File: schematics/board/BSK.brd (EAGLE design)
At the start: 94 x 94 mm, 47 parts

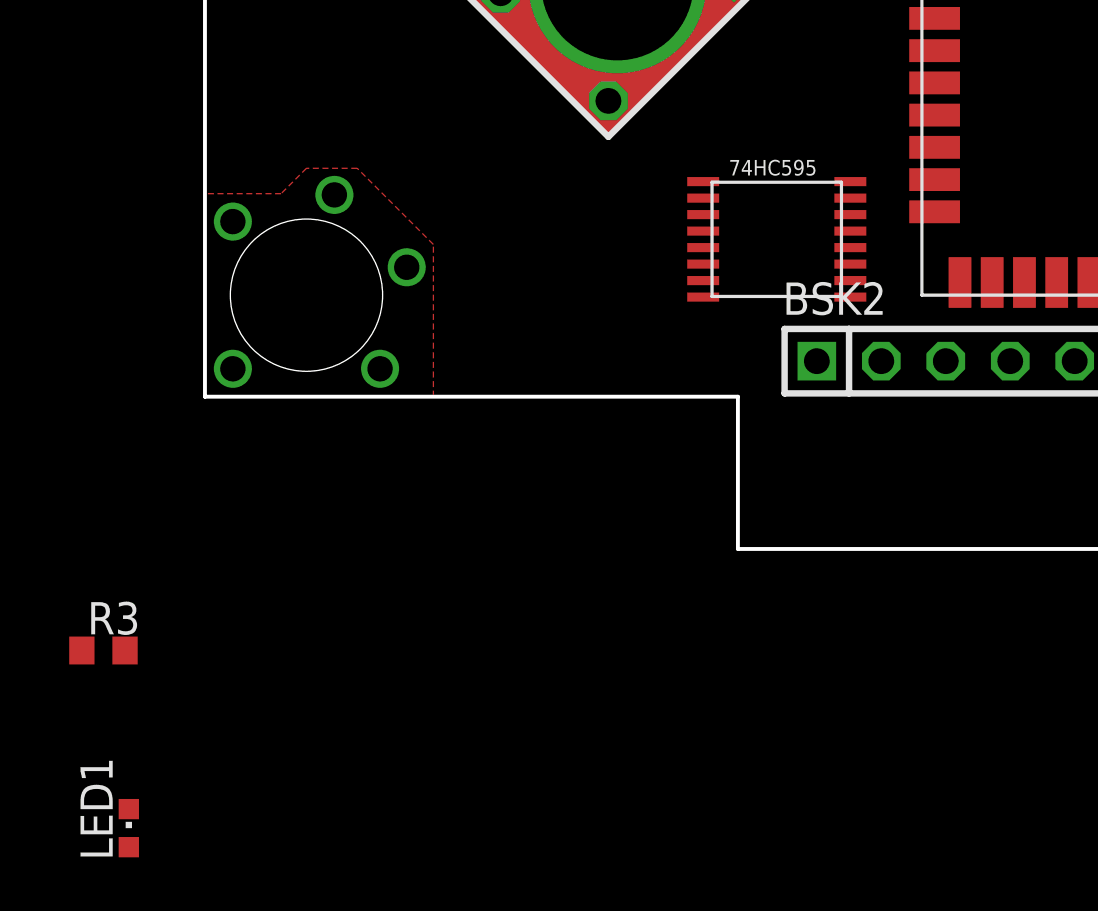
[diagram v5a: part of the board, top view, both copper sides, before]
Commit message: обновлена схема БКУ
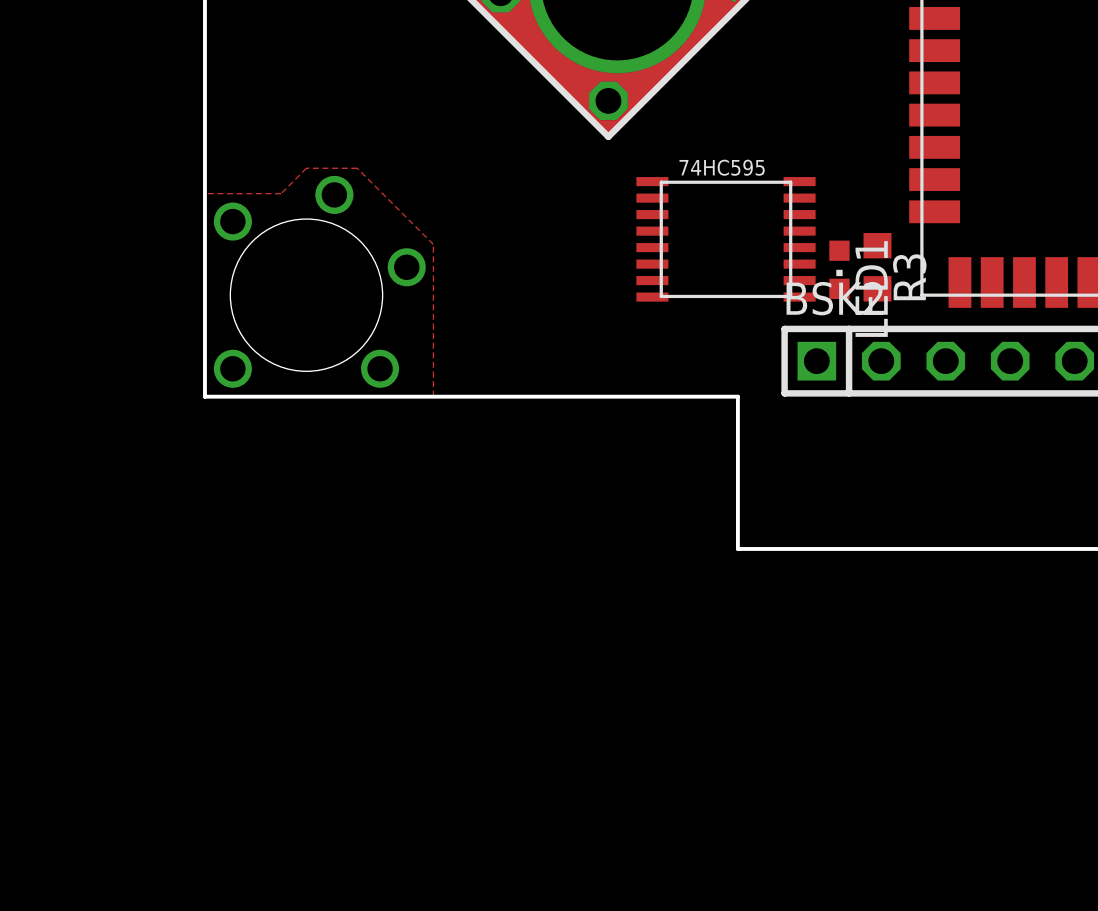
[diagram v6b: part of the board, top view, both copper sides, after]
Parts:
- moved LED1 35.6 mm to (31.0, 11.0), turned to 180 degrees
- moved R3 34.0 mm to (32.5, 11.1), turned to 270 degrees
- moved U$15 2.00 mm to (26.5, 12.2)
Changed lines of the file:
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@@
 <attribute name="VALUE" x="82.635" y="56.105" size="1.27" layer="27" rot="R180"/>
 </element>
-<element name="U$15" library="CanCubeSat" package="74HC595" value="74HC595" x="28.53" y="12.2" smashed="yes"/>
+<element name="U$15" library="CanCubeSat" package="74HC595" value="74HC595" x="26.53" y="12.2" smashed="yes"/>
 <element name="U$17" library="CanCubeSat" package="74HC595" value="74HC595" x="79.53" y="33.85" smashed="yes"/>
 <element name="BSK3" library="pinheadCS" package="1X12" value="" x="86.6" y="47" smashed="yes" rot="R90">
@@
 </element>
 <element name="U$22" library="CanCubeSat" package="FS8205A+" value="FS8205A+" x="78.8" y="55.3" smashed="yes"/>
-<element name="R3" library="resistor" library_urn="urn:adsk.eagle:library:348" package="R0603" package3d_urn="urn:adsk.eagle:package:23555/3" value="2k" x="2" y="-4" smashed="yes">
-<attribute name="NAME" x="1.365" y="-3.365" size="1.27" layer="25"/>
-<attribute name="VALUE" x="1.365" y="-5.905" size="1.27" layer="27"/>
-</element>
-<element name="LED1" library="led" library_urn="urn:adsk.eagle:library:259" package="CHIPLED_0603" package3d_urn="urn:adsk.eagle:package:15822/2" value="" x="3" y="-11" smashed="yes">
-<attribute name="NAME" x="2.365" y="-12.27" size="1.27" layer="25" rot="R90"/>
-<attribute name="POPULARITY" value="28" x="-3" y="-4" size="1.778" layer="27" display="off"/>
-<attribute name="VALUE" x="4.905" y="-12.27" size="1.27" layer="27" rot="R90"/>
+<element name="R3" library="resistor" library_urn="urn:adsk.eagle:library:348" package="R0603" package3d_urn="urn:adsk.eagle:package:23555/3" value="2k" x="32.5" y="11.1" smashed="yes" rot="R270">
+<attribute name="NAME" x="33.135" y="11.735" size="1.27" layer="25" rot="R270"/>
+<attribute name="VALUE" x="30.595" y="11.735" size="1.27" layer="27" rot="R270"/>
+</element>
+<element name="LED1" library="led" library_urn="urn:adsk.eagle:library:259" package="CHIPLED_0603" package3d_urn="urn:adsk.eagle:package:15822/2" value="" x="31" y="11" smashed="yes" rot="R180">
+<attribute name="NAME" x="31.635" y="12.27" size="1.27" layer="25" rot="R270"/>
+<attribute name="POPULARITY" value="28" x="37" y="4" size="1.778" layer="27" rot="R180" display="off"/>
+<attribute name="VALUE" x="29.095" y="12.27" size="1.27" layer="27" rot="R270"/>
 </element>
 </elements>
@@
 <wire x1="82.43" y1="32.225" x2="71.43" y2="13.805" width="0" layer="19" extent="1-1"/>
 <wire x1="82.43" y1="36.125" x2="82.43" y2="32.225" width="0" layer="19" extent="1-1"/>
-<wire x1="31.43" y1="14.475" x2="50.99" y2="27.5" width="0" layer="19" extent="1-1"/>
-<wire x1="31.43" y1="10.575" x2="31.43" y2="14.475" width="0" layer="19" extent="1-1"/>
-<wire x1="3" y1="-11.75" x2="31.43" y2="10.575" width="0" layer="19" extent="1-1"/>
+<wire x1="29.43" y1="14.475" x2="50.99" y2="27.5" width="0" layer="19" extent="1-1"/>
+<wire x1="31" y1="11.75" x2="29.43" y2="14.475" width="0" layer="19" extent="1-1"/>
+<wire x1="29.43" y1="10.575" x2="31" y2="11.75" width="0" layer="19" extent="1-1"/>
 </signal>
 <signal name="GND">
@@
 <wire x1="61.15" y1="20" x2="62.85" y2="17.9" width="0" layer="19" extent="1-1"/>
 <wire x1="61.15" y1="22.1" x2="61.15" y2="20" width="0" layer="19" extent="1-1"/>
-<wire x1="31.43" y1="12.525" x2="34.75" y2="24.715" width="0" layer="19" extent="1-1"/>
-<wire x1="30.11" y1="7.4" x2="31.43" y2="12.525" width="0" layer="19" extent="1-1"/>
-<wire x1="25.63" y1="9.925" x2="30.11" y2="7.4" width="0" layer="19" extent="1-1"/>
+<wire x1="29.43" y1="12.525" x2="34.75" y2="24.715" width="0" layer="19" extent="1-1"/>
+<wire x1="30.11" y1="7.4" x2="29.43" y2="12.525" width="0" layer="19" extent="1-1"/>
+<wire x1="23.63" y1="9.925" x2="29.43" y2="12.525" width="0" layer="19" extent="1-1"/>
 <wire x1="21.114" y1="57.785" x2="41.1" y2="67" width="0" layer="19" extent="1-1"/>
 <wire x1="7.4" y1="61.89" x2="21.114" y2="57.785" width="0" layer="19" extent="1-1"/>
@@
 <contactref element="U$15" pad="2"/>
 <contactref element="BSK2A" pad="3"/>
-<wire x1="25.63" y1="13.825" x2="7.4" y2="56.81" width="0" layer="19" extent="1-1"/>
+<wire x1="23.63" y1="13.825" x2="7.4" y2="56.81" width="0" layer="19" extent="1-1"/>
 </signal>
 <signal name="B2A_KEM-">
 <contactref element="U$15" pad="3"/>
 <contactref element="BSK2A" pad="2"/>
-<wire x1="25.63" y1="13.175" x2="7.4" y2="59.35" width="0" layer="19" extent="1-1"/>
+<wire x1="23.63" y1="13.175" x2="7.4" y2="59.35" width="0" layer="19" extent="1-1"/>
 </signal>
 <signal name="B2A_KHEAT">
 <contactref element="U$15" pad="1"/>
 <contactref element="BSK2A" pad="4"/>
-<wire x1="25.63" y1="14.475" x2="7.4" y2="54.27" width="0" layer="19" extent="1-1"/>
+<wire x1="23.63" y1="14.475" x2="7.4" y2="54.27" width="0" layer="19" extent="1-1"/>
 </signal>
 <signal name="B3_KEM+">
@@
 <contactref element="BSK4" pad="12"/>
 <contactref element="U$15" pad="5"/>
-<wire x1="25.63" y1="11.875" x2="35.57" y2="86.6" width="0" layer="19" extent="1-1"/>
+<wire x1="23.63" y1="11.875" x2="35.57" y2="86.6" width="0" layer="19" extent="1-1"/>
 </signal>
 <signal name="B5_KEM+">
@@
 <contactref element="U$15" pad="15"/>
 <contactref element="BSK2A" pad="5"/>
-<wire x1="31.43" y1="13.825" x2="7.4" y2="51.73" width="0" layer="19" extent="1-1"/>
+<wire x1="29.43" y1="13.825" x2="7.4" y2="51.73" width="0" layer="19" extent="1-1"/>
 </signal>
 <signal name="B3_KVCC">
@@
 <contactref element="BSK4" pad="13"/>
 <contactref element="U$15" pad="4"/>
-<wire x1="25.63" y1="12.525" x2="33.03" y2="86.6" width="0" layer="19" extent="1-1"/>
+<wire x1="23.63" y1="12.525" x2="33.03" y2="86.6" width="0" layer="19" extent="1-1"/>
 </signal>
 <signal name="N$24">
@@
 <contactref element="U$9" pad="9"/>
 <contactref element="U$15" pad="14"/>
-<wire x1="31.43" y1="13.175" x2="71.43" y2="9.255" width="0" layer="19" extent="1-1"/>
+<wire x1="29.43" y1="13.175" x2="71.43" y2="9.255" width="0" layer="19" extent="1-1"/>
 </signal>
 <signal name="N$20">
 <contactref element="U$15" pad="9"/>
 <contactref element="U$17" pad="14"/>
-<wire x1="31.43" y1="9.925" x2="82.43" y2="34.825" width="0" layer="19" extent="1-1"/>
+<wire x1="29.43" y1="9.925" x2="82.43" y2="34.825" width="0" layer="19" extent="1-1"/>
 </signal>
 <signal name="STCP">
@@
 <wire x1="71.43" y1="11.205" x2="82.43" y2="33.525" width="0" layer="19" extent="1-1"/>
 <wire x1="39.56" y1="27.5" x2="71.43" y2="11.205" width="0" layer="19" extent="1-1"/>
-<wire x1="31.43" y1="11.875" x2="39.56" y2="27.5" width="0" layer="19" extent="1-1"/>
+<wire x1="29.43" y1="11.875" x2="39.56" y2="27.5" width="0" layer="19" extent="1-1"/>
 </signal>
 <signal name="SHCP">
@@
 <wire x1="71.43" y1="10.555" x2="82.43" y2="32.875" width="0" layer="19" extent="1-1"/>
 <wire x1="40.83" y1="27.5" x2="71.43" y2="10.555" width="0" layer="19" extent="1-1"/>
-<wire x1="31.43" y1="11.225" x2="40.83" y2="27.5" width="0" layer="19" extent="1-1"/>
+<wire x1="29.43" y1="11.225" x2="40.83" y2="27.5" width="0" layer="19" extent="1-1"/>
 </signal>
 <signal name="DS">
@@
 <contactref element="BSK4" pad="11"/>
 <contactref element="U$15" pad="6"/>
-<wire x1="25.63" y1="11.225" x2="38.11" y2="86.6" width="0" layer="19" extent="1-1"/>
+<wire x1="23.63" y1="11.225" x2="38.11" y2="86.6" width="0" layer="19" extent="1-1"/>
 </signal>
 <signal name="B4_KEM-">
 <contactref element="BSK4" pad="10"/>
 <contactref element="U$15" pad="7"/>
-<wire x1="25.63" y1="10.575" x2="40.65" y2="86.6" width="0" layer="19" extent="1-1"/>
+<wire x1="23.63" y1="10.575" x2="40.65" y2="86.6" width="0" layer="19" extent="1-1"/>
 </signal>
 <signal name="HEAT1">
@@
 <contactref element="R3" pad="1"/>
 <contactref element="U$13" pad="30"/>
-<wire x1="1.15" y1="-4" x2="42.1" y2="10.5" width="0" layer="19" extent="1-1"/>
+<wire x1="32.5" y1="11.95" x2="42.1" y2="10.5" width="0" layer="19" extent="1-1"/>
 </signal>
 <signal name="N$34">
 <contactref element="LED1" pad="C"/>
 <contactref element="R3" pad="2"/>
-<wire x1="2.85" y1="-4" x2="3" y2="-10.25" width="0" layer="19" extent="1-1"/>
+<wire x1="32.5" y1="10.25" x2="31" y2="10.25" width="0" layer="19" extent="1-1"/>
 </signal>
 </signals>

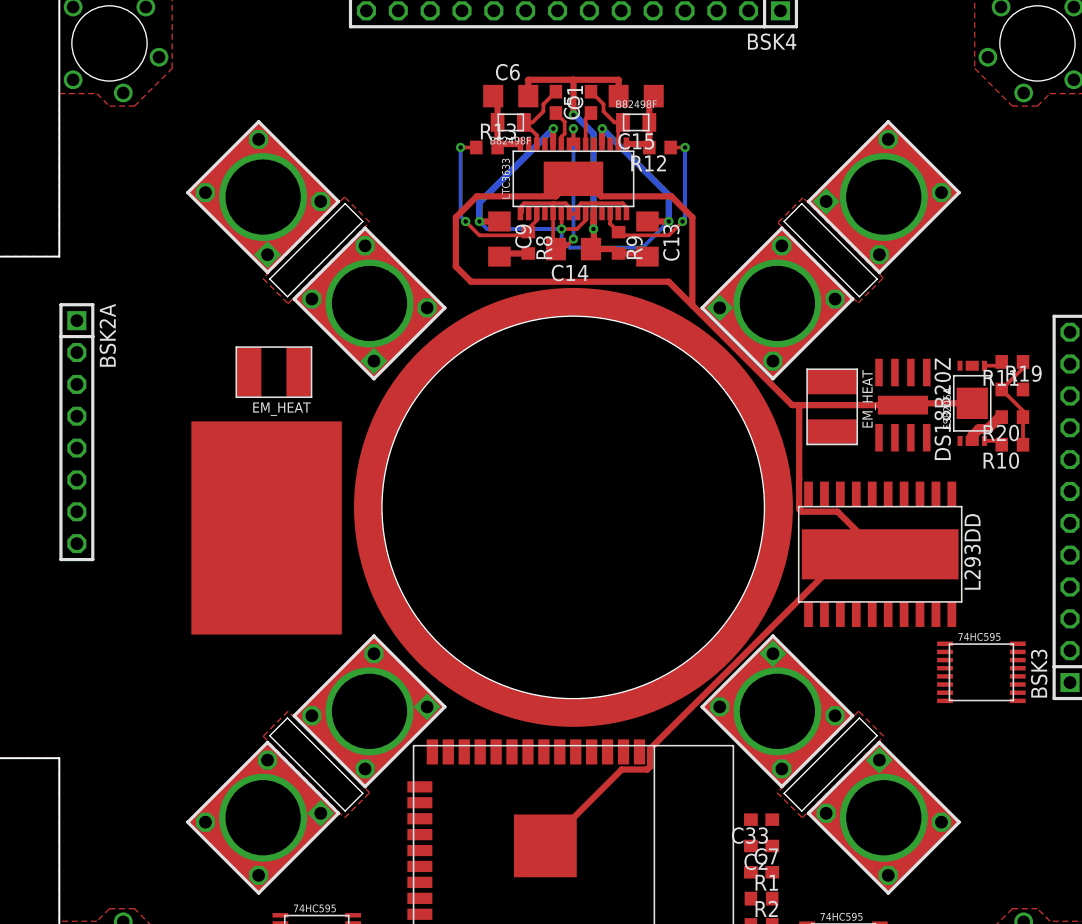
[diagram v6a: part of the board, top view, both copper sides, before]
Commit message: Добавлены светодиоды на платы БСК
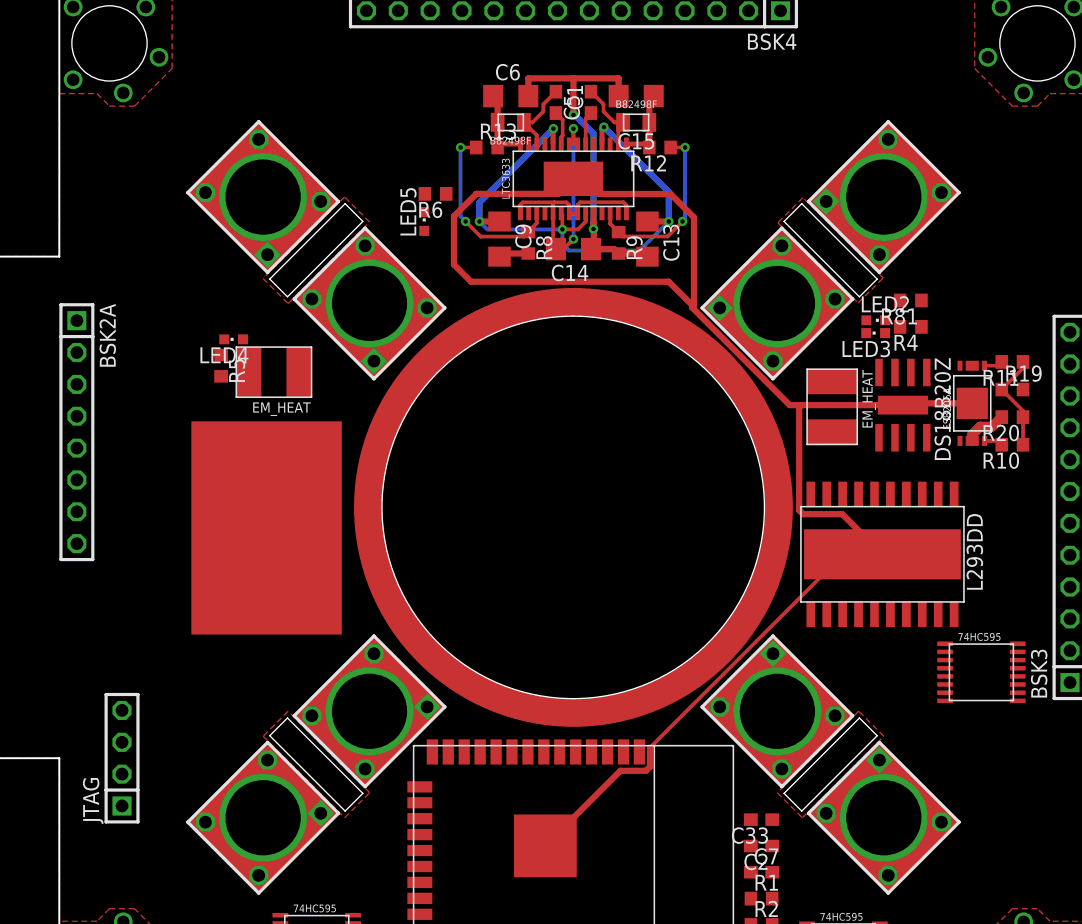
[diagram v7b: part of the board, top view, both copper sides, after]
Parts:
- added JTAG: (no value), pinheadCS:1X04
- added LED2, LED3, LED4, LED5: (no value), led:CHIPLED_0603
- added R4, R5, R6, R81: 2k, resistor:R0603
- R2: value 5k -> 5k1
- moved U$8 0.18 mm to (71.6, 43.3)
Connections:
- new net MTCK: JTAG.3, U$13.16
- new net MTDI: JTAG.4, U$13.14
- new net MTDO: JTAG.1, U$13.23
- new net MTMS: JTAG.2, U$13.13
- new net N$35: LED2.C, R81.2
- new net N$36: LED3.A, R4.2
- new net N$37: LED4.C, R5.1
- new net N$38: LED5.C, R6.2
- net 5V: now also R6.1
- net BUS-: now also LED5.A
- net GND: now also R5.2
- net N$1: now also LED2.A, LED3.C
- net N$2: now also R4.1, R81.1
- net N$3: now also LED4.A
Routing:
- net GND: track 161.9 -> 163.5 mm
- net BUS+: track 46.5 -> 47.2 mm
- net N$24: track 27.4 -> 28.0 mm

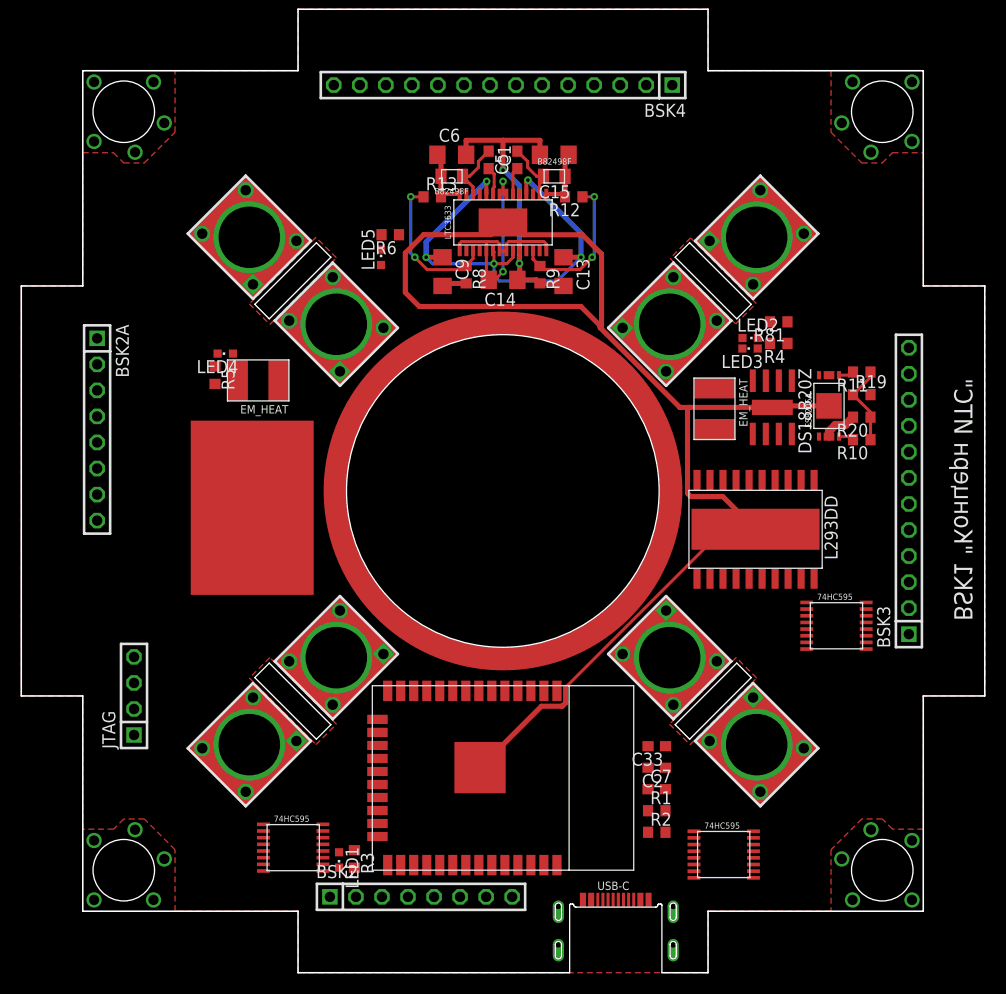
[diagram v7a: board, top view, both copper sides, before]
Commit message: Разведена БСК1
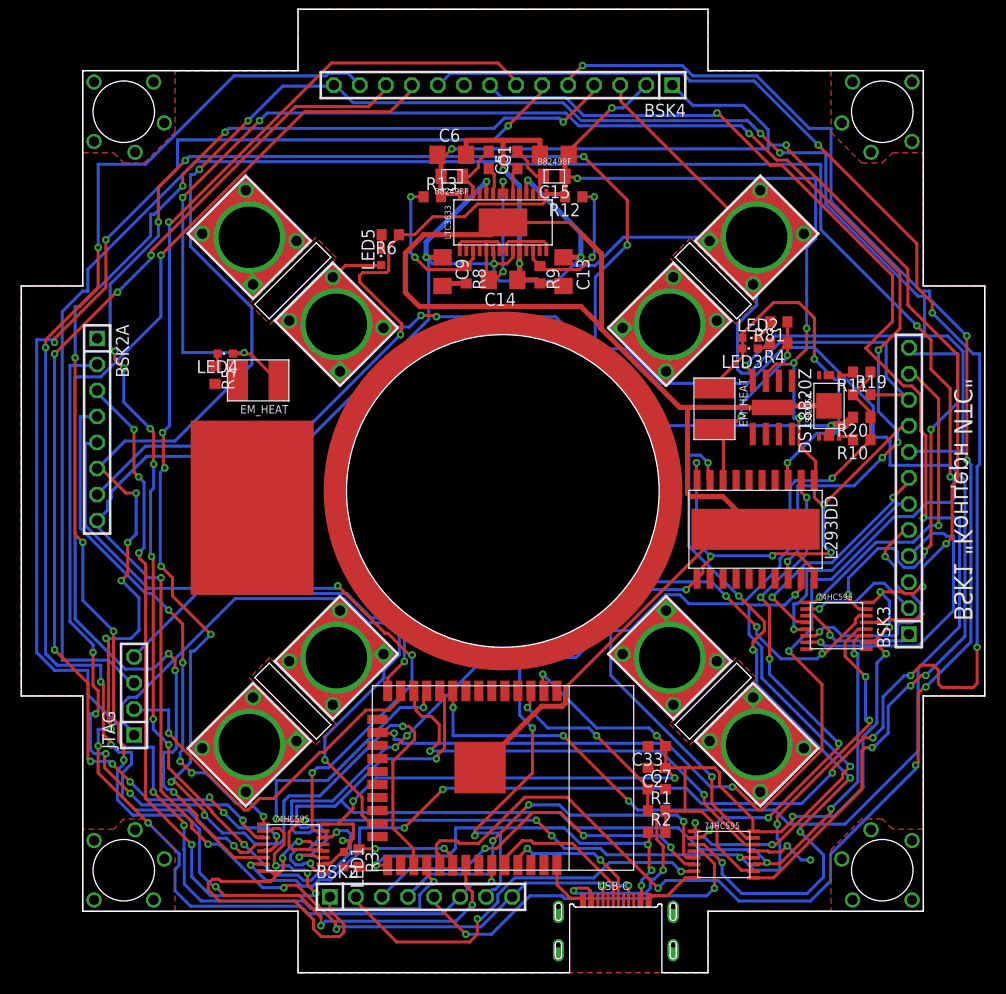
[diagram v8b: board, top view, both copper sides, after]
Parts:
- moved LED1 0.49 mm to (31.5, 11.0)
- moved R3 0.46 mm to (33.0, 11.2)
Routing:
- net 1W: track 0.00 -> 258.2 mm, vias 0 -> 13
- net N$19: track 0.00 -> 251.0 mm, vias 0 -> 16
- net MTCK: track 0.00 -> 247.0 mm, vias 0 -> 5
- net 5V: track 6.60 -> 243.4 mm, vias 0 -> 14
- net VDD: track 6.37 -> 242.8 mm, vias 0 -> 13
- net BUS+: track 47.2 -> 272.4 mm, vias 5 -> 11
- net B4_KEM-: track 0.00 -> 188.5 mm, vias 0 -> 9
- net I2CINT: track 0.00 -> 163.0 mm, vias 0 -> 6
- net TIME: track 0.00 -> 160.2 mm, vias 0 -> 10
- net PL_KVCC: track 0.00 -> 159.2 mm, vias 0 -> 5
- net SDATM: track 0.00 -> 156.5 mm, vias 0 -> 6
- net SCLTM: track 0.00 -> 148.9 mm, vias 0 -> 8
- net N$3: track 0.00 -> 145.8 mm, vias 0 -> 8
- net B4_KVCC: track 0.00 -> 116.9 mm, vias 0 -> 5
- net STCP: track 0.00 -> 112.1 mm, vias 0 -> 9
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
